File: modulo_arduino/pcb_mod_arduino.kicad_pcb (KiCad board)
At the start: 2 copper layers, 116 x 100 mm, 76 parts, among them J1 modulo 1, J2 modulo 2, J3 modulo 3, J4 modulo 4, J5 modulo 5, J6 modulo 6, J7 power

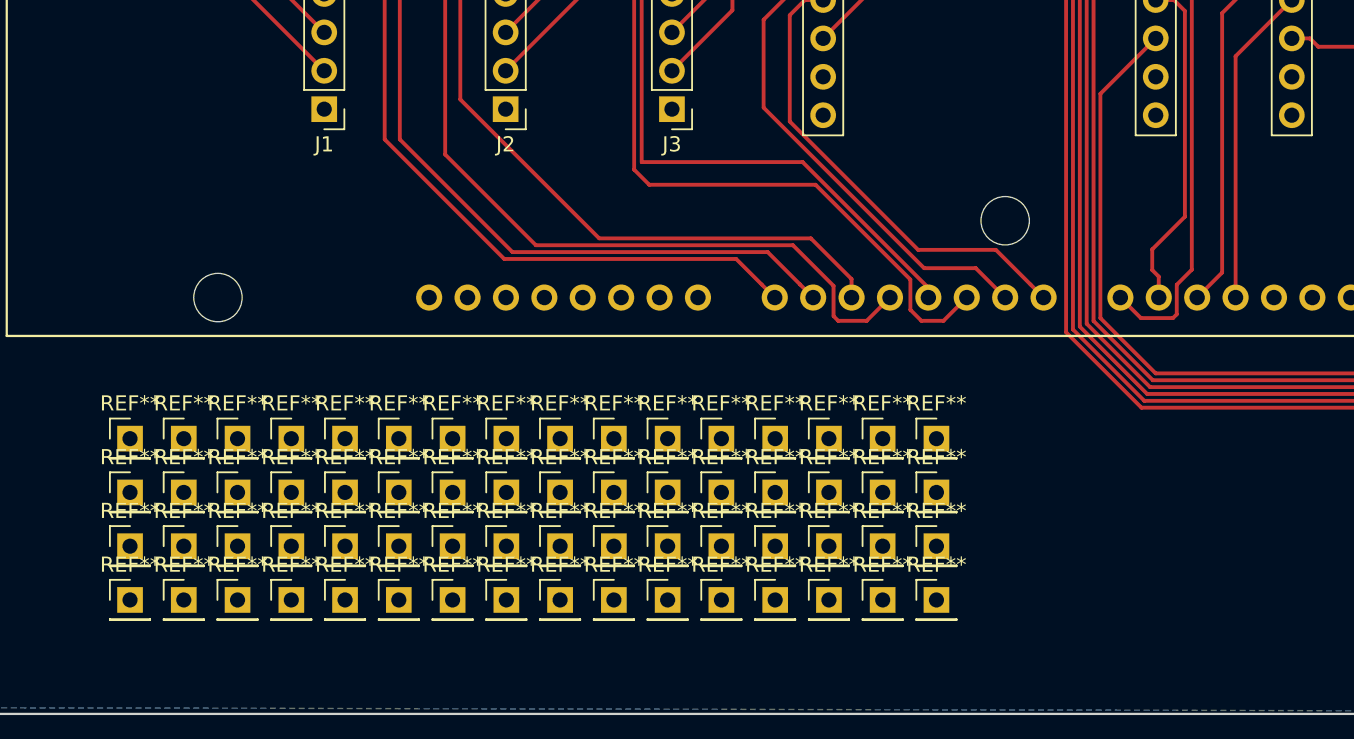
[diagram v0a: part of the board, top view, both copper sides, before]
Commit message: marcas en pin #1 de headers, primer gerber export :3
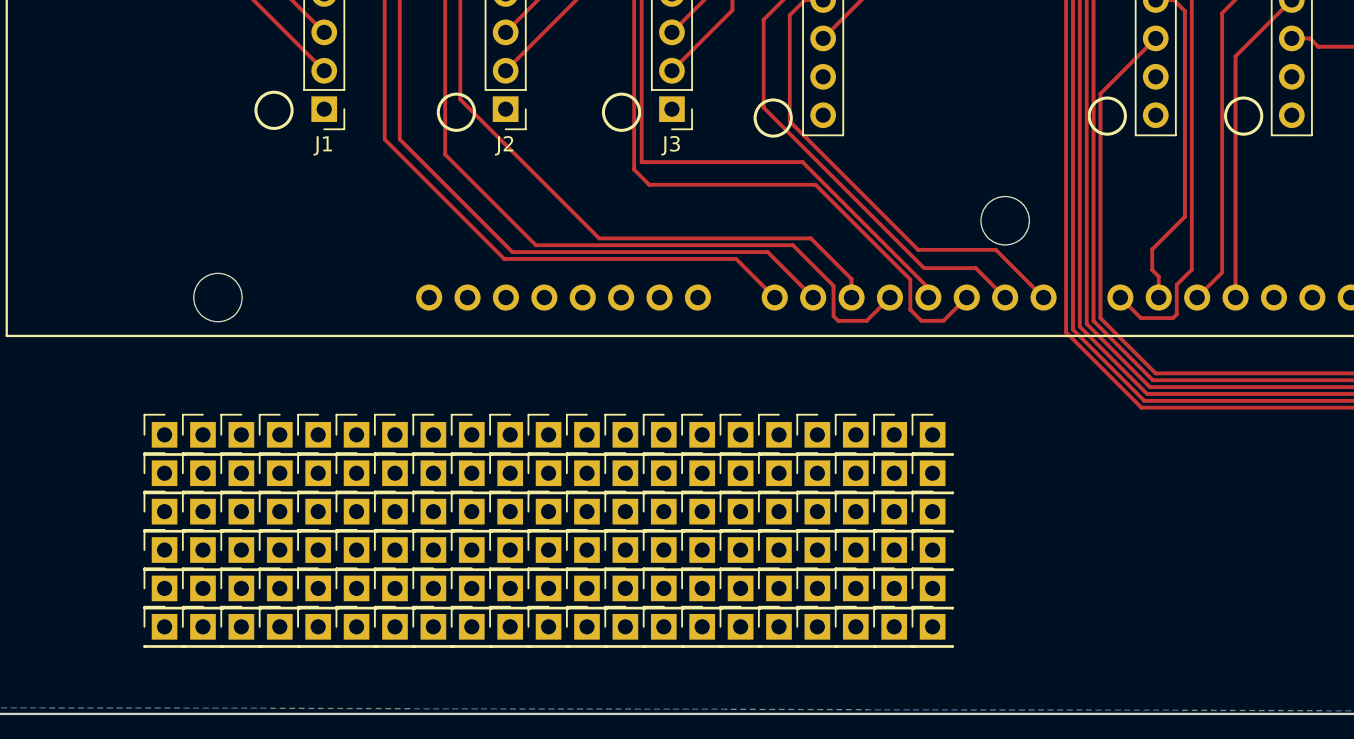
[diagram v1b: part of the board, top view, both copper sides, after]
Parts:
- removed the REF** at (117.6, 129.8)
- removed the REF** at (121.2, 140.5)
- removed the REF** at (124.7, 140.5)
- removed the REF** at (128.3, 140.5)
- removed the REF** at (128.3, 136.9)
- removed the REF** at (124.7, 136.9)
- removed the REF** at (121.2, 136.9)
- removed the REF** at (117.6, 136.9)
- removed the REF** at (131.8, 136.9)
- removed the REF** at (135.4, 136.9)
- removed the REF** at (138.9, 136.9)
- removed the REF** at (121.2, 129.8)
- removed the REF** at (142.5, 136.9)
- removed the REF** at (138.9, 140.5)
- removed the REF** at (135.4, 140.5)
- removed the REF** at (131.8, 140.5)
- removed the REF** at (131.8, 133.3)
- removed the REF** at (135.4, 133.3)
- removed the REF** at (138.9, 133.3)
- removed the REF** at (142.5, 133.3)
- removed the REF** at (142.5, 129.8)
- removed the REF** at (124.7, 129.8)
- removed the REF** at (138.9, 129.8)
- removed the REF** at (135.4, 129.8)
- removed the REF** at (131.8, 129.8)
- removed the REF** at (103.4, 129.8)
- removed the REF** at (106.9, 129.8)
- removed the REF** at (110.5, 129.8)
- removed the REF** at (114.0, 129.8)
- removed the REF** at (114.0, 133.3)
- removed the REF** at (110.5, 133.3)
- removed the REF** at (106.9, 133.3)
- removed the REF** at (128.3, 129.8)
- removed the REF** at (103.4, 133.3)
- removed the REF** at (103.4, 140.5)
- removed the REF** at (106.9, 140.5)
- removed the REF** at (110.5, 140.5)
- removed the REF** at (114.0, 140.5)
- removed the REF** at (114.0, 136.9)
- removed the REF** at (110.5, 136.9)
- removed the REF** at (106.9, 136.9)
- removed the REF** at (103.4, 136.9)
- removed the REF** at (89.2, 136.9)
- removed the REF** at (128.3, 133.3)
- removed the REF** at (92.7, 136.9)
- removed the REF** at (96.3, 136.9)
- removed the REF** at (99.8, 136.9)
- removed the REF** at (99.8, 140.5)
- removed the REF** at (96.3, 140.5)
- removed the REF** at (92.7, 140.5)
- removed the REF** at (89.2, 140.5)
- removed the REF** at (89.2, 133.3)
- removed the REF** at (92.7, 133.3)
- removed the REF** at (96.3, 133.3)
- removed the REF** at (124.7, 133.3)
- removed the REF** at (99.8, 133.3)
- removed the REF** at (99.8, 129.8)
- removed the REF** at (96.3, 129.8)
- removed the REF** at (92.7, 129.8)
- removed the REF** at (89.2, 129.8)
- removed the REF** at (121.2, 133.3)
- removed the REF** at (117.6, 133.3)
- removed the REF** at (117.6, 140.5)
- added ?: , Pin_Headers:Pin_Header_Straight_1x01_Pitch2.54mm, F.Cu at (99.1, 142.2)
- added ?: , Pin_Headers:Pin_Header_Straight_1x01_Pitch2.54mm, F.Cu at (96.5, 132.1)
- added ?: , Pin_Headers:Pin_Header_Straight_1x01_Pitch2.54mm, F.Cu at (127.0, 134.6)
- added ?: , Pin_Headers:Pin_Header_Straight_1x01_Pitch2.54mm, F.Cu at (127.0, 139.7)
- added ?: , Pin_Headers:Pin_Header_Straight_1x01_Pitch2.54mm, F.Cu at (127.0, 142.2)
- added ?: , Pin_Headers:Pin_Header_Straight_1x01_Pitch2.54mm, F.Cu at (137.2, 142.2)
- added ?: , Pin_Headers:Pin_Header_Straight_1x01_Pitch2.54mm, F.Cu at (137.2, 139.7)
- added ?: , Pin_Headers:Pin_Header_Straight_1x01_Pitch2.54mm, F.Cu at (137.2, 134.6)
- added ?: , Pin_Headers:Pin_Header_Straight_1x01_Pitch2.54mm, F.Cu at (137.2, 137.2)
- added ?: , Pin_Headers:Pin_Header_Straight_1x01_Pitch2.54mm, F.Cu at (134.6, 137.2)
- added ?: , Pin_Headers:Pin_Header_Straight_1x01_Pitch2.54mm, F.Cu at (134.6, 134.6)
- added ?: , Pin_Headers:Pin_Header_Straight_1x01_Pitch2.54mm, F.Cu at (134.6, 139.7)
- added ?: , Pin_Headers:Pin_Header_Straight_1x01_Pitch2.54mm, F.Cu at (99.1, 132.1)
- added ?: , Pin_Headers:Pin_Header_Straight_1x01_Pitch2.54mm, F.Cu at (134.6, 142.2)
- added ?: , Pin_Headers:Pin_Header_Straight_1x01_Pitch2.54mm, F.Cu at (134.6, 129.5)
- added ?: , Pin_Headers:Pin_Header_Straight_1x01_Pitch2.54mm, F.Cu at (134.6, 132.1)
- added ?: , Pin_Headers:Pin_Header_Straight_1x01_Pitch2.54mm, F.Cu at (137.2, 132.1)
- added ?: , Pin_Headers:Pin_Header_Straight_1x01_Pitch2.54mm, F.Cu at (137.2, 129.5)
- added ?: , Pin_Headers:Pin_Header_Straight_1x01_Pitch2.54mm, F.Cu at (142.2, 129.5)
- added ?: , Pin_Headers:Pin_Header_Straight_1x01_Pitch2.54mm, F.Cu at (142.2, 132.1)
- added ?: , Pin_Headers:Pin_Header_Straight_1x01_Pitch2.54mm, F.Cu at (139.7, 132.1)
- added ?: , Pin_Headers:Pin_Header_Straight_1x01_Pitch2.54mm, F.Cu at (139.7, 129.5)
- added ?: , Pin_Headers:Pin_Header_Straight_1x01_Pitch2.54mm, F.Cu at (139.7, 142.2)
- added ?: , Pin_Headers:Pin_Header_Straight_1x01_Pitch2.54mm, F.Cu at (99.1, 129.5)
- added ?: , Pin_Headers:Pin_Header_Straight_1x01_Pitch2.54mm, F.Cu at (139.7, 139.7)
- added ?: , Pin_Headers:Pin_Header_Straight_1x01_Pitch2.54mm, F.Cu at (139.7, 134.6)
- added ?: , Pin_Headers:Pin_Header_Straight_1x01_Pitch2.54mm, F.Cu at (139.7, 137.2)
- added ?: , Pin_Headers:Pin_Header_Straight_1x01_Pitch2.54mm, F.Cu at (142.2, 137.2)
- added ?: , Pin_Headers:Pin_Header_Straight_1x01_Pitch2.54mm, F.Cu at (142.2, 134.6)
- added ?: , Pin_Headers:Pin_Header_Straight_1x01_Pitch2.54mm, F.Cu at (142.2, 139.7)
- added ?: , Pin_Headers:Pin_Header_Straight_1x01_Pitch2.54mm, F.Cu at (94.0, 129.5)
- added ?: , Pin_Headers:Pin_Header_Straight_1x01_Pitch2.54mm, F.Cu at (94.0, 132.1)
- added ?: , Pin_Headers:Pin_Header_Straight_1x01_Pitch2.54mm, F.Cu at (91.4, 132.1)
- added ?: , Pin_Headers:Pin_Header_Straight_1x01_Pitch2.54mm, F.Cu at (91.4, 129.5)
- added ?: , Pin_Headers:Pin_Header_Straight_1x01_Pitch2.54mm, F.Cu at (91.4, 142.2)
- added ?: , Pin_Headers:Pin_Header_Straight_1x01_Pitch2.54mm, F.Cu at (91.4, 139.7)
- added ?: , Pin_Headers:Pin_Header_Straight_1x01_Pitch2.54mm, F.Cu at (91.4, 134.6)
- added ?: , Pin_Headers:Pin_Header_Straight_1x01_Pitch2.54mm, F.Cu at (99.1, 139.7)
- added ?: , Pin_Headers:Pin_Header_Straight_1x01_Pitch2.54mm, F.Cu at (91.4, 137.2)
- added ?: , Pin_Headers:Pin_Header_Straight_1x01_Pitch2.54mm, F.Cu at (94.0, 137.2)
- added ?: , Pin_Headers:Pin_Header_Straight_1x01_Pitch2.54mm, F.Cu at (94.0, 134.6)
- added ?: , Pin_Headers:Pin_Header_Straight_1x01_Pitch2.54mm, F.Cu at (94.0, 139.7)
- added ?: , Pin_Headers:Pin_Header_Straight_1x01_Pitch2.54mm, F.Cu at (94.0, 142.2)
- added ?: , Pin_Headers:Pin_Header_Straight_1x01_Pitch2.54mm, F.Cu at (101.6, 137.2)
- added ?: , Pin_Headers:Pin_Header_Straight_1x01_Pitch2.54mm, F.Cu at (101.6, 134.6)
- added ?: , Pin_Headers:Pin_Header_Straight_1x01_Pitch2.54mm, F.Cu at (101.6, 139.7)
- added ?: , Pin_Headers:Pin_Header_Straight_1x01_Pitch2.54mm, F.Cu at (101.6, 142.2)
- added ?: , Pin_Headers:Pin_Header_Straight_1x01_Pitch2.54mm, F.Cu at (101.6, 129.5)
- added ?: , Pin_Headers:Pin_Header_Straight_1x01_Pitch2.54mm, F.Cu at (99.1, 134.6)
- added ?: , Pin_Headers:Pin_Header_Straight_1x01_Pitch2.54mm, F.Cu at (101.6, 132.1)
- added ?: , Pin_Headers:Pin_Header_Straight_1x01_Pitch2.54mm, F.Cu at (121.9, 142.2)
- added ?: , Pin_Headers:Pin_Header_Straight_1x01_Pitch2.54mm, F.Cu at (121.9, 139.7)
- added ?: , Pin_Headers:Pin_Header_Straight_1x01_Pitch2.54mm, F.Cu at (121.9, 134.6)
- added ?: , Pin_Headers:Pin_Header_Straight_1x01_Pitch2.54mm, F.Cu at (121.9, 137.2)
- added ?: , Pin_Headers:Pin_Header_Straight_1x01_Pitch2.54mm, F.Cu at (119.4, 137.2)
- added ?: , Pin_Headers:Pin_Header_Straight_1x01_Pitch2.54mm, F.Cu at (119.4, 134.6)
- added ?: , Pin_Headers:Pin_Header_Straight_1x01_Pitch2.54mm, F.Cu at (119.4, 139.7)
- added ?: , Pin_Headers:Pin_Header_Straight_1x01_Pitch2.54mm, F.Cu at (119.4, 142.2)
- added ?: , Pin_Headers:Pin_Header_Straight_1x01_Pitch2.54mm, F.Cu at (119.4, 129.5)
- added ?: , Pin_Headers:Pin_Header_Straight_1x01_Pitch2.54mm, F.Cu at (99.1, 137.2)
- added ?: , Pin_Headers:Pin_Header_Straight_1x01_Pitch2.54mm, F.Cu at (119.4, 132.1)
- added ?: , Pin_Headers:Pin_Header_Straight_1x01_Pitch2.54mm, F.Cu at (121.9, 132.1)
- added ?: , Pin_Headers:Pin_Header_Straight_1x01_Pitch2.54mm, F.Cu at (121.9, 129.5)
- added ?: , Pin_Headers:Pin_Header_Straight_1x01_Pitch2.54mm, F.Cu at (116.8, 129.5)
- added ?: , Pin_Headers:Pin_Header_Straight_1x01_Pitch2.54mm, F.Cu at (116.8, 132.1)
- added ?: , Pin_Headers:Pin_Header_Straight_1x01_Pitch2.54mm, F.Cu at (114.3, 132.1)
- added ?: , Pin_Headers:Pin_Header_Straight_1x01_Pitch2.54mm, F.Cu at (114.3, 129.5)
- added ?: , Pin_Headers:Pin_Header_Straight_1x01_Pitch2.54mm, F.Cu at (114.3, 142.2)
- added ?: , Pin_Headers:Pin_Header_Straight_1x01_Pitch2.54mm, F.Cu at (114.3, 139.7)
- added ?: , Pin_Headers:Pin_Header_Straight_1x01_Pitch2.54mm, F.Cu at (114.3, 134.6)
- added ?: , Pin_Headers:Pin_Header_Straight_1x01_Pitch2.54mm, F.Cu at (96.5, 137.2)
- added ?: , Pin_Headers:Pin_Header_Straight_1x01_Pitch2.54mm, F.Cu at (114.3, 137.2)
- added ?: , Pin_Headers:Pin_Header_Straight_1x01_Pitch2.54mm, F.Cu at (116.8, 137.2)
- added ?: , Pin_Headers:Pin_Header_Straight_1x01_Pitch2.54mm, F.Cu at (116.8, 134.6)
- added ?: , Pin_Headers:Pin_Header_Straight_1x01_Pitch2.54mm, F.Cu at (116.8, 139.7)
- added ?: , Pin_Headers:Pin_Header_Straight_1x01_Pitch2.54mm, F.Cu at (116.8, 142.2)
- added ?: , Pin_Headers:Pin_Header_Straight_1x01_Pitch2.54mm, F.Cu at (106.7, 142.2)
- added ?: , Pin_Headers:Pin_Header_Straight_1x01_Pitch2.54mm, F.Cu at (106.7, 139.7)
- added ?: , Pin_Headers:Pin_Header_Straight_1x01_Pitch2.54mm, F.Cu at (106.7, 134.6)
- added ?: , Pin_Headers:Pin_Header_Straight_1x01_Pitch2.54mm, F.Cu at (106.7, 137.2)
- added ?: , Pin_Headers:Pin_Header_Straight_1x01_Pitch2.54mm, F.Cu at (104.1, 137.2)
- added ?: , Pin_Headers:Pin_Header_Straight_1x01_Pitch2.54mm, F.Cu at (96.5, 134.6)
- added ?: , Pin_Headers:Pin_Header_Straight_1x01_Pitch2.54mm, F.Cu at (104.1, 134.6)
- added ?: , Pin_Headers:Pin_Header_Straight_1x01_Pitch2.54mm, F.Cu at (104.1, 139.7)
- added ?: , Pin_Headers:Pin_Header_Straight_1x01_Pitch2.54mm, F.Cu at (104.1, 142.2)
- added ?: , Pin_Headers:Pin_Header_Straight_1x01_Pitch2.54mm, F.Cu at (104.1, 129.5)
- added ?: , Pin_Headers:Pin_Header_Straight_1x01_Pitch2.54mm, F.Cu at (104.1, 132.1)
- added ?: , Pin_Headers:Pin_Header_Straight_1x01_Pitch2.54mm, F.Cu at (106.7, 132.1)
- added ?: , Pin_Headers:Pin_Header_Straight_1x01_Pitch2.54mm, F.Cu at (106.7, 129.5)
- added ?: , Pin_Headers:Pin_Header_Straight_1x01_Pitch2.54mm, F.Cu at (111.8, 129.5)
- added ?: , Pin_Headers:Pin_Header_Straight_1x01_Pitch2.54mm, F.Cu at (111.8, 132.1)
- added ?: , Pin_Headers:Pin_Header_Straight_1x01_Pitch2.54mm, F.Cu at (109.2, 132.1)
- added ?: , Pin_Headers:Pin_Header_Straight_1x01_Pitch2.54mm, F.Cu at (96.5, 139.7)
- added ?: , Pin_Headers:Pin_Header_Straight_1x01_Pitch2.54mm, F.Cu at (109.2, 129.5)
- added ?: , Pin_Headers:Pin_Header_Straight_1x01_Pitch2.54mm, F.Cu at (109.2, 142.2)
- added ?: , Pin_Headers:Pin_Header_Straight_1x01_Pitch2.54mm, F.Cu at (109.2, 139.7)
- added ?: , Pin_Headers:Pin_Header_Straight_1x01_Pitch2.54mm, F.Cu at (109.2, 134.6)
- added ?: , Pin_Headers:Pin_Header_Straight_1x01_Pitch2.54mm, F.Cu at (109.2, 137.2)
- added ?: , Pin_Headers:Pin_Header_Straight_1x01_Pitch2.54mm, F.Cu at (111.8, 137.2)
- added ?: , Pin_Headers:Pin_Header_Straight_1x01_Pitch2.54mm, F.Cu at (111.8, 134.6)
- added ?: , Pin_Headers:Pin_Header_Straight_1x01_Pitch2.54mm, F.Cu at (111.8, 139.7)
- added ?: , Pin_Headers:Pin_Header_Straight_1x01_Pitch2.54mm, F.Cu at (111.8, 142.2)
- added ?: , Pin_Headers:Pin_Header_Straight_1x01_Pitch2.54mm, F.Cu at (132.1, 142.2)
- added ?: , Pin_Headers:Pin_Header_Straight_1x01_Pitch2.54mm, F.Cu at (96.5, 142.2)
- added ?: , Pin_Headers:Pin_Header_Straight_1x01_Pitch2.54mm, F.Cu at (132.1, 139.7)
- added ?: , Pin_Headers:Pin_Header_Straight_1x01_Pitch2.54mm, F.Cu at (132.1, 134.6)
- added ?: , Pin_Headers:Pin_Header_Straight_1x01_Pitch2.54mm, F.Cu at (132.1, 137.2)
- added ?: , Pin_Headers:Pin_Header_Straight_1x01_Pitch2.54mm, F.Cu at (129.5, 137.2)
- added ?: , Pin_Headers:Pin_Header_Straight_1x01_Pitch2.54mm, F.Cu at (129.5, 134.6)
- added ?: , Pin_Headers:Pin_Header_Straight_1x01_Pitch2.54mm, F.Cu at (129.5, 139.7)
- added ?: , Pin_Headers:Pin_Header_Straight_1x01_Pitch2.54mm, F.Cu at (129.5, 142.2)
- added ?: , Pin_Headers:Pin_Header_Straight_1x01_Pitch2.54mm, F.Cu at (129.5, 129.5)
- added ?: , Pin_Headers:Pin_Header_Straight_1x01_Pitch2.54mm, F.Cu at (129.5, 132.1)
- added ?: , Pin_Headers:Pin_Header_Straight_1x01_Pitch2.54mm, F.Cu at (132.1, 132.1)
- added ?: , Pin_Headers:Pin_Header_Straight_1x01_Pitch2.54mm, F.Cu at (96.5, 129.5)
- added ?: , Pin_Headers:Pin_Header_Straight_1x01_Pitch2.54mm, F.Cu at (132.1, 129.5)
- added ?: , Pin_Headers:Pin_Header_Straight_1x01_Pitch2.54mm, F.Cu at (127.0, 129.5)
- added ?: , Pin_Headers:Pin_Header_Straight_1x01_Pitch2.54mm, F.Cu at (127.0, 132.1)
- added ?: , Pin_Headers:Pin_Header_Straight_1x01_Pitch2.54mm, F.Cu at (124.5, 132.1)
- added ?: , Pin_Headers:Pin_Header_Straight_1x01_Pitch2.54mm, F.Cu at (124.5, 129.5)
- added ?: , Pin_Headers:Pin_Header_Straight_1x01_Pitch2.54mm, F.Cu at (124.5, 142.2)
- added ?: , Pin_Headers:Pin_Header_Straight_1x01_Pitch2.54mm, F.Cu at (124.5, 139.7)
- added ?: , Pin_Headers:Pin_Header_Straight_1x01_Pitch2.54mm, F.Cu at (124.5, 134.6)
- added ?: , Pin_Headers:Pin_Header_Straight_1x01_Pitch2.54mm, F.Cu at (124.5, 137.2)
- added ?: , Pin_Headers:Pin_Header_Straight_1x01_Pitch2.54mm, F.Cu at (127.0, 137.2)
- moved ? 1.80 mm to (142.2, 142.2)
- renumbered REF** to ?

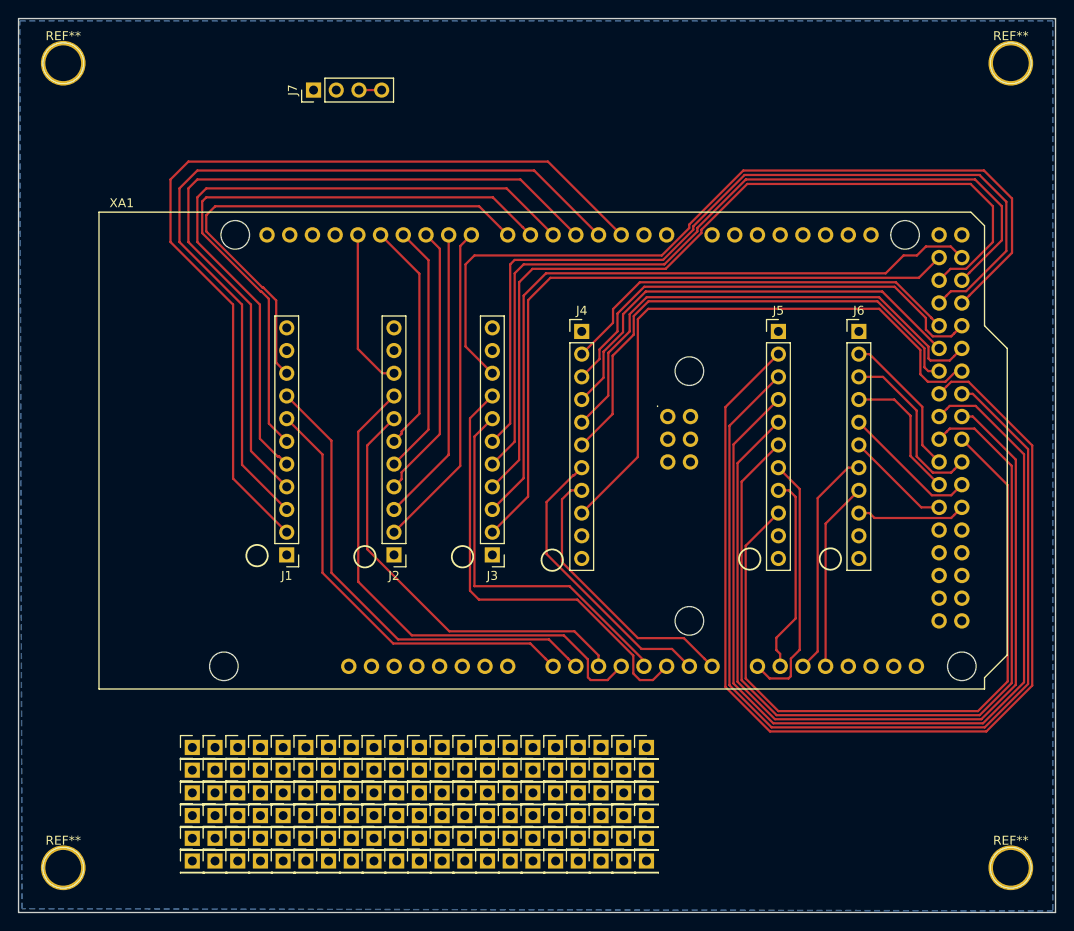
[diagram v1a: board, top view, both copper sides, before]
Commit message: marcas pines, reemplazo borneras, orientacion, separacion headers, ubicacion arduino
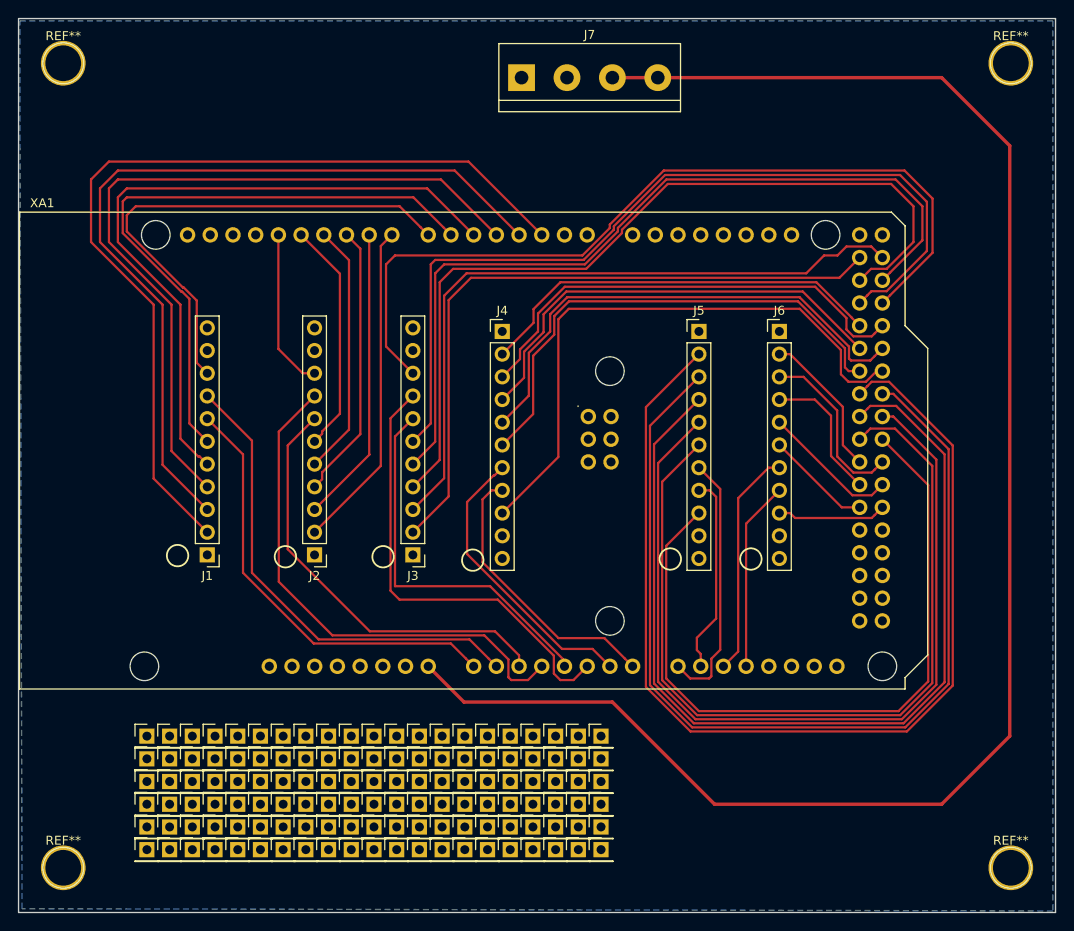
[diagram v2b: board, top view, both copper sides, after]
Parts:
- J7: footprint Pin_Headers:Pin_Header_Straight_1x04_Pitch2.54mm -> Connectors_Terminal_Blocks:TerminalBlock_bornier-4_P5.08mm
- moved J7 23.3 mm to (128.3, 54.6), turned to 0 degrees
- moved J1 8.89 mm to (93.1, 108.0)
- moved J2 8.89 mm to (105.1, 108.0)
- moved J3 8.89 mm to (116.1, 108.0)
- moved J4 8.89 mm to (126.1, 83.0)
- moved XA1 8.89 mm to (72.1, 123.0)
- moved J5 8.89 mm to (148.1, 83.0)
- moved J6 8.89 mm to (157.1, 83.0)
- moved ? 5.24 mm to (129.5, 135.9)
- moved ? 5.24 mm to (129.5, 133.3)
- moved ? 5.24 mm to (129.5, 141.0)
- moved ? 5.24 mm to (129.5, 130.8)
- moved ? 5.24 mm to (137.2, 130.8)
- moved ? 5.24 mm to (137.2, 135.9)
- moved ? 5.24 mm to (137.2, 133.3)
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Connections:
- XA1 pad VIN: Net-(XA1-PadVIN) -> +5V
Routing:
- net +5V: track 2.54 -> 188.2 mm

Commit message: marcas botones ok, gerber exports ultima version
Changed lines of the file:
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@@
   )
   (setup
-    (last_trace_width 0.381)
+    (last_trace_width 0.25)
     (user_trace_width 0.1524)
     (user_trace_width 0.254)
@@
     (visible_elements FFFFFF7F)
     (pcbplotparams
-      (layerselection 0x01030_80000001)
+      (layerselection 0x31030_80000001)
       (usegerberextensions false)
       (excludeedgelayer true)
@@
     )
   )
-  (gr_circle (center 153.924 108.458) (end 154.559 109.474) (layer F.SilkS) (width 0.2))
-  (gr_circle (center 144.907 108.458) (end 145.542 109.474) (layer F.SilkS) (width 0.2))
-  (gr_circle (center 122.809 108.585) (end 123.444 109.601) (layer F.SilkS) (width 0.2))
+  (gr_circle (center 153.162 82.804) (end 153.797 83.82) (layer F.SilkS) (width 0.2))
+  (gr_circle (center 144.145 82.804) (end 144.78 83.82) (layer F.SilkS) (width 0.2))
+  (gr_circle (center 122.809 82.931) (end 123.444 83.947) (layer F.SilkS) (width 0.2))
   (gr_circle (center 112.776 108.204) (end 113.411 109.22) (layer F.SilkS) (width 0.2))
   (gr_circle (center 101.854 108.204) (end 102.489 109.22) (layer F.SilkS) (width 0.2))
